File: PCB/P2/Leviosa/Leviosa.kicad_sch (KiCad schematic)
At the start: 56 parts, among them J1 Barrel_Jack, J2 2.54mm 1x03 Spare

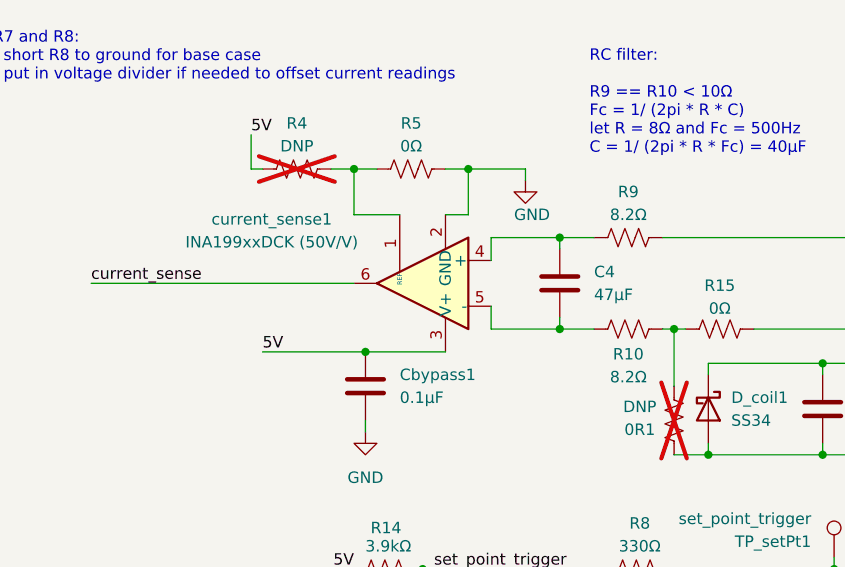
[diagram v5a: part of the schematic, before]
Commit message: updated schematic for usb and i2s
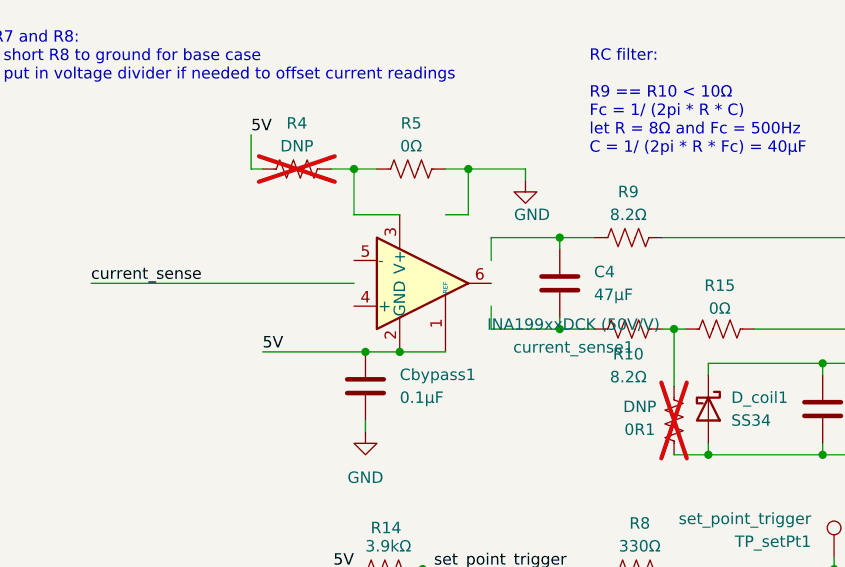
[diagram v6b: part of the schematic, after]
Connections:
- net 5V: now also current_sense1.1 (REF), current_sense1.2 (GND); no longer current_sense1.3 (V+)
- net GND: no longer current_sense1.2 (GND)
- net current_sense: no longer current_sense1.6
- net at C4.2, R10.2: no longer current_sense1.5 (-)
- net at R4.1, R5.2: now also current_sense1.3 (V+); no longer current_sense1.1 (REF)
- net at C4.1, R9.2: no longer current_sense1.4 (+)
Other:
- moved on the sheet: current_sense1
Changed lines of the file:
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@@
+	)
+	(junction
+		(at 187.96 60.96)
+		(diameter 0)
+		(color 0 0 0 0)
 	)
 	(junction
@@
 	(wire
 		(pts
-			(xy 184.15 60.96) (xy 193.04 60.96)
+			(xy 184.15 60.96) (xy 187.96 60.96)
 		)
 		(stroke
@@
 		(pts
 			(xy 83.82 45.72) (xy 83.82 49.53)
+		)
+		(stroke
+			(width 0)
+			(type default)
+		)
+	)
+	(wire
+		(pts
+			(xy 187.96 60.96) (xy 193.04 60.96)
 		)
 		(stroke
@@
 	(symbol
 		(lib_id "Amplifier_Current:INA199xxDCK")
-		(at 190.5 53.34 180)
+		(at 190.5 53.34 0)
 		(unit 1)
 		(exclude_from_sim no)
@@
 		(dnp no)
 		(property "Reference" "current_sense1"
-			(at 173.736 46.228 0)
+			(at 207.264 60.452 0)
 			(effects
 				(font
@@
 		)
 		(property "Value" "INA199xxDCK (50V/V)"
-			(at 173.736 48.768 0)
+			(at 207.264 57.912 0)
 			(effects
 				(font
@@
 		)
 		(property "Footprint" "Package_TO_SOT_SMD:SOT-363_SC-70-6"
-			(at 189.23 54.61 0)
+			(at 191.77 52.07 0)
 			(effects
 				(font
@@
 		)
 		(property "Datasheet" "http://www.ti.com/lit/ds/symlink/ina199.pdf"
-			(at 186.69 57.15 0)
-			(effects
-				(font
+			(at 194.31 49.53 0)
+			(effects
+				(font
